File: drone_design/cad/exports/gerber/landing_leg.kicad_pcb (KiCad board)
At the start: 2 copper layers, 40 x 81 mm, 0 parts

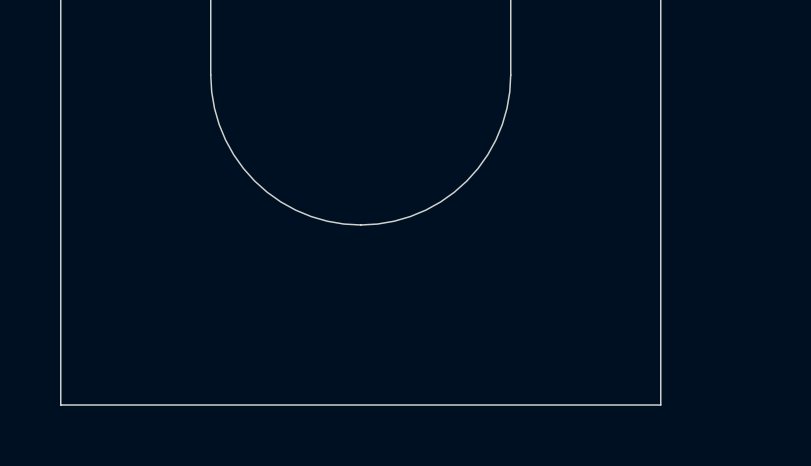
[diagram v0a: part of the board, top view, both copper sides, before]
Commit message: feat: fix ToF bracket alignment, add motor mount to arm tips
- Fix all 6 ToF sensor/bracket positions with correct rotations
  so sensors sit flush against bracket tab faces, sensing outward
- Add circular motor mounting plate at arm tips (25mm dia)
  with 4x M2 bolt holes on 16mm circle + center shaft clearance
- Add matching M2 threaded holes to motor base plate model
- Rebuild all STLs and viewer (68 parts, 15.8 MB total)
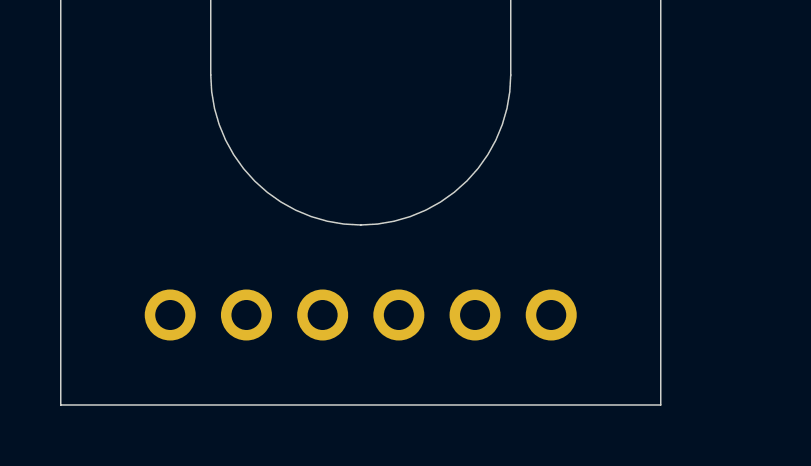
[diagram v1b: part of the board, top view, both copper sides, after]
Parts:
- added ?: , MountingHole:MountingHole_1.0mm, F.Cu at (-6.35, 77.0)
- added ?: , MountingHole:MountingHole_1.0mm, F.Cu at (-3.81, 77.0)
- added ?: , MountingHole:MountingHole_1.0mm, F.Cu at (-1.27, 77.0)
- added ?: , MountingHole:MountingHole_1.0mm, F.Cu at (1.27, 77.0)
- added ?: , MountingHole:MountingHole_1.0mm, F.Cu at (3.81, 77.0)
- added ?: , MountingHole:MountingHole_1.0mm, F.Cu at (6.35, 77.0)
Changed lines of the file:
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@@
   (gr_line (start 0.0000 56.0000) (end 0.0000 56.0000) (layer "Edge.Cuts") (width 0.05))
   (gr_line (start 5.0000 61.0000) (end 5.0000 69.0000) (layer "Edge.Cuts") (width 0.05))
+  (footprint "MountingHole:MountingHole_1.0mm" (layer "F.Cu")
+    (at -6.3500 77.0000)
+    (pad "" thru_hole circle (at 0 0) (size 1.70 1.70) (drill 1.00)
+      (layers "*.Cu" "*.Mask")
+    )
+  )
+  (footprint "MountingHole:MountingHole_1.0mm" (layer "F.Cu")
+    (at -3.8100 77.0000)
+    (pad "" thru_hole circle (at 0 0) (size 1.70 1.70) (drill 1.00)
+      (layers "*.Cu" "*.Mask")
+    )
+  )
+  (footprint "MountingHole:MountingHole_1.0mm" (layer "F.Cu")
+    (at -1.2700 77.0000)
+    (pad "" thru_hole circle (at 0 0) (size 1.70 1.70) (drill 1.00)
+      (layers "*.Cu" "*.Mask")
+    )
+  )
+  (footprint "MountingHole:MountingHole_1.0mm" (layer "F.Cu")
+    (at 1.2700 77.0000)
+    (pad "" thru_hole circle (at 0 0) (size 1.70 1.70) (drill 1.00)
+      (layers "*.Cu" "*.Mask")
+    )
+  )
+  (footprint "MountingHole:MountingHole_1.0mm" (layer "F.Cu")
+    (at 3.8100 77.0000)
+    (pad "" thru_hole circle (at 0 0) (size 1.70 1.70) (drill 1.00)
+      (layers "*.Cu" "*.Mask")
+    )
+  )
+  (footprint "MountingHole:MountingHole_1.0mm" (layer "F.Cu")
+    (at 6.3500 77.0000)
+    (pad "" thru_hole circle (at 0 0) (size 1.70 1.70) (drill 1.00)
+      (layers "*.Cu" "*.Mask")
+    )
+  )
   (gr_text "LEG" (at 0.0000 40.0000) (layer "F.SilkS")
     (effects (font (size 2 2) (thickness 0.2)))

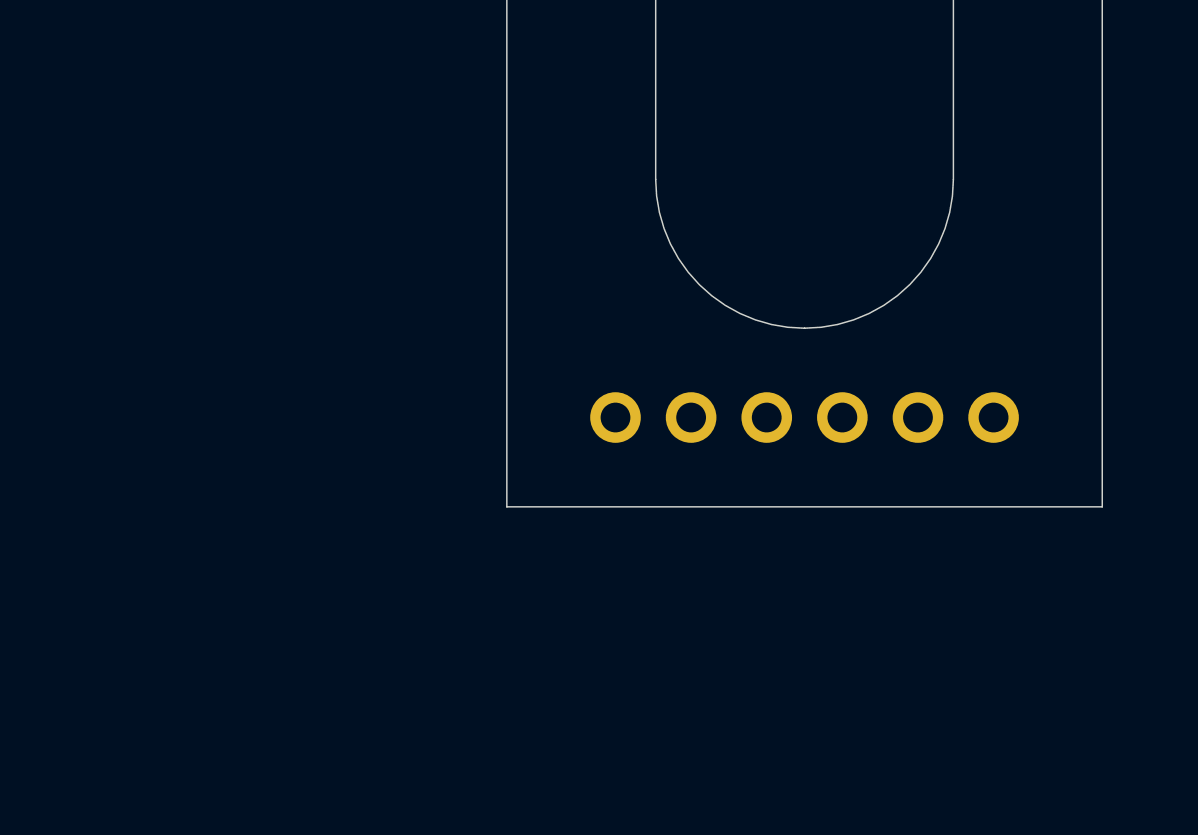
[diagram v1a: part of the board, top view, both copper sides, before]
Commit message: feat: modular two-section arms and nose boom with adjustable length
Arms split into inner (tab) + outer (motor) sections with 40mm
I-beam overlap zone. 4x M2 slider holes at 10mm pitch allow
adjustable motor distance. Same pattern for nose boom: root (190mm)
+ tip (230mm) sections with web/collar interlock.

- arm.py: make_arm_inner(), make_arm_outer(), make_arm() (compat)
- nose_boom.py: make_boom_root(), make_boom_tip(), make_nose_boom()
- export_stl.py: add arm_inner, arm_outer, boom_root, boom_tip
  as individual exportable parts with COMPONENT_CATALOG metadata
- Refactored drone_3d_model.py with assembly_constants module
- All 23 individual parts + 49 assembly parts export cleanly
- Removed obsolete drone_3d_model.scad
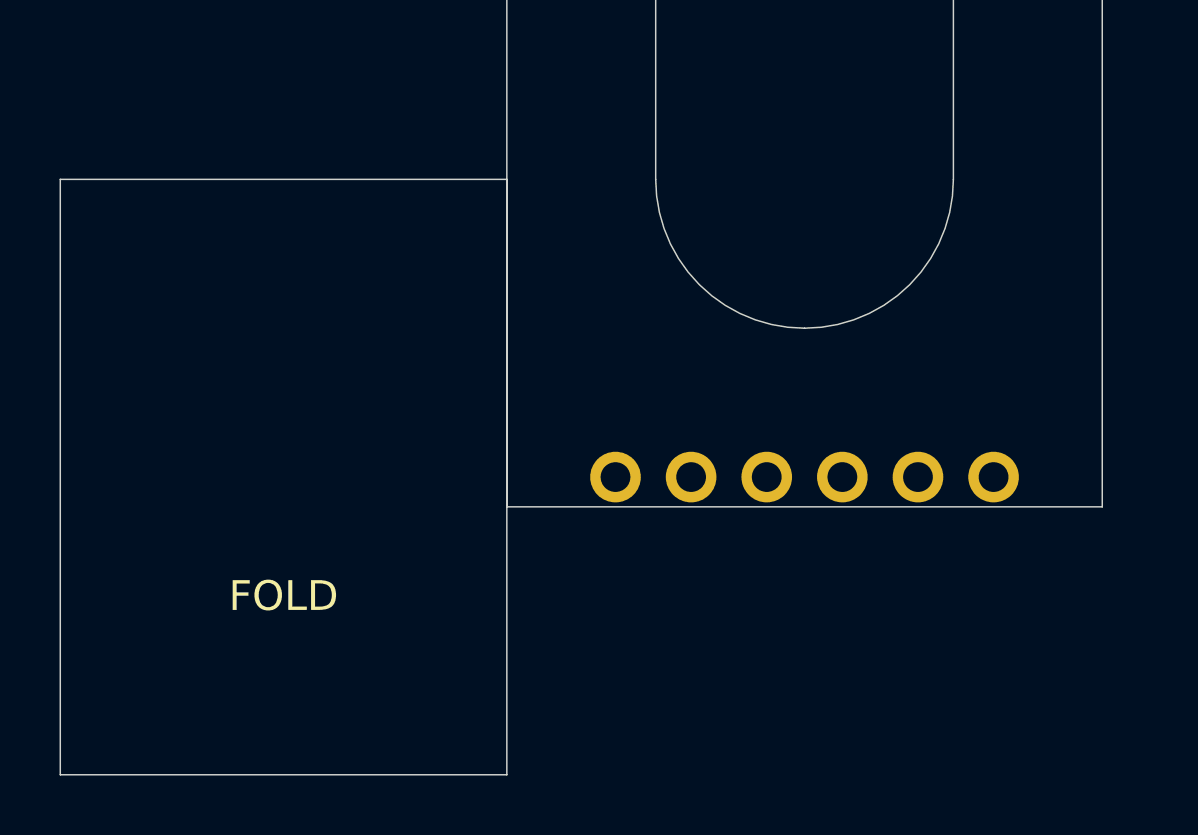
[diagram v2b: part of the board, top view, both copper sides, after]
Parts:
- removed the ? at (-6.35, 77.0)
- removed the ? at (-3.81, 77.0)
- removed the ? at (-1.27, 77.0)
- removed the ? at (1.27, 77.0)
- removed the ? at (3.81, 77.0)
- removed the ? at (6.35, 77.0)
- added ?: , MountingHole:MountingHole_1.0mm, F.Cu at (-6.35, 79.0)
- added ?: , MountingHole:MountingHole_1.0mm, F.Cu at (-3.81, 79.0)
- added ?: , MountingHole:MountingHole_1.0mm, F.Cu at (-1.27, 79.0)
- added ?: , MountingHole:MountingHole_1.0mm, F.Cu at (1.27, 79.0)
- added ?: , MountingHole:MountingHole_1.0mm, F.Cu at (3.81, 79.0)
- added ?: , MountingHole:MountingHole_1.0mm, F.Cu at (6.35, 79.0)
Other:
- board size 40 x 81 mm -> 55 x 90 mm
- board text added: "FOLD"
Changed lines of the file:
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@@
   (paper "A4")
   (title_block
-    (title "Drone Landing Leg (L-shape)")
+    (title "Drone Landing Leg (L-shape + Tab)")
     (date "2026-03-14")
     (comment 1 "Material: FR4")
@@
   (gr_line (start 30.0000 1.0000) (end -10.0000 1.0000) (layer "Edge.Cuts") (width 0.05))
   (gr_line (start -10.0000 1.0000) (end -10.0000 -1.0000) (layer "Edge.Cuts") (width 0.05))
+  (gr_line (start -25.0000 69.0000) (end -10.0000 69.0000) (layer "Edge.Cuts") (width 0.05))
+  (gr_line (start -10.0000 69.0000) (end -10.0000 89.0000) (layer "Edge.Cuts") (width 0.05))
+  (gr_line (start -10.0000 89.0000) (end -25.0000 89.0000) (layer "Edge.Cuts") (width 0.05))
+  (gr_line (start -25.0000 89.0000) (end -25.0000 69.0000) (layer "Edge.Cuts") (width 0.05))
   (gr_arc (start 5.0000 29.0000) (mid 3.5355 32.5355) (end 0.0000 34.0000) (layer "Edge.Cuts") (width 0.05))
   (gr_arc (start 0.0000 34.0000) (mid -3.5355 32.5355) (end -5.0000 29.0000) (layer "Edge.Cuts") (width 0.05))
@@
   (gr_line (start 5.0000 61.0000) (end 5.0000 69.0000) (layer "Edge.Cuts") (width 0.05))
   (footprint "MountingHole:MountingHole_1.0mm" (layer "F.Cu")
-    (at -6.3500 77.0000)
+    (at -6.3500 79.0000)
     (pad "" thru_hole circle (at 0 0) (size 1.70 1.70) (drill 1.00)
       (layers "*.Cu" "*.Mask")
@@
   )
   (footprint "MountingHole:MountingHole_1.0mm" (layer "F.Cu")
-    (at -3.8100 77.0000)
+    (at -3.8100 79.0000)
     (pad "" thru_hole circle (at 0 0) (size 1.70 1.70) (drill 1.00)
       (layers "*.Cu" "*.Mask")
@@
   )
   (footprint "MountingHole:MountingHole_1.0mm" (layer "F.Cu")
-    (at -1.2700 77.0000)
+    (at -1.2700 79.0000)
     (pad "" thru_hole circle (at 0 0) (size 1.70 1.70) (drill 1.00)
       (layers "*.Cu" "*.Mask")
@@
   )
   (footprint "MountingHole:MountingHole_1.0mm" (layer "F.Cu")
-    (at 1.2700 77.0000)
+    (at 1.2700 79.0000)
     (pad "" thru_hole circle (at 0 0) (size 1.70 1.70) (drill 1.00)
       (layers "*.Cu" "*.Mask")
@@
   )
   (footprint "MountingHole:MountingHole_1.0mm" (layer "F.Cu")
-    (at 3.8100 77.0000)
+    (at 3.8100 79.0000)
     (pad "" thru_hole circle (at 0 0) (size 1.70 1.70) (drill 1.00)
       (layers "*.Cu" "*.Mask")
@@
   )
   (footprint "MountingHole:MountingHole_1.0mm" (layer "F.Cu")
-    (at 6.3500 77.0000)
+    (at 6.3500 79.0000)
     (pad "" thru_hole circle (at 0 0) (size 1.70 1.70) (drill 1.00)
       (layers "*.Cu" "*.Mask")
     )
   )
+  (gr_text "FOLD" (at -17.5000 83.0000) (layer "F.SilkS")
+    (effects (font (size 1.0 1.0) (thickness 0.12)))
+  )
   (gr_text "LEG" (at 0.0000 40.0000) (layer "F.SilkS")
